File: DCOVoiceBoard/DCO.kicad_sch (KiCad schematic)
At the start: 72 parts, among them Q201 BC857, Q202 BC857, U201 TL074, U202 TL074, U203 MCP4451-104E-ST, U204 TL074, U205 MCP4451-104E-ST, U206 TL072

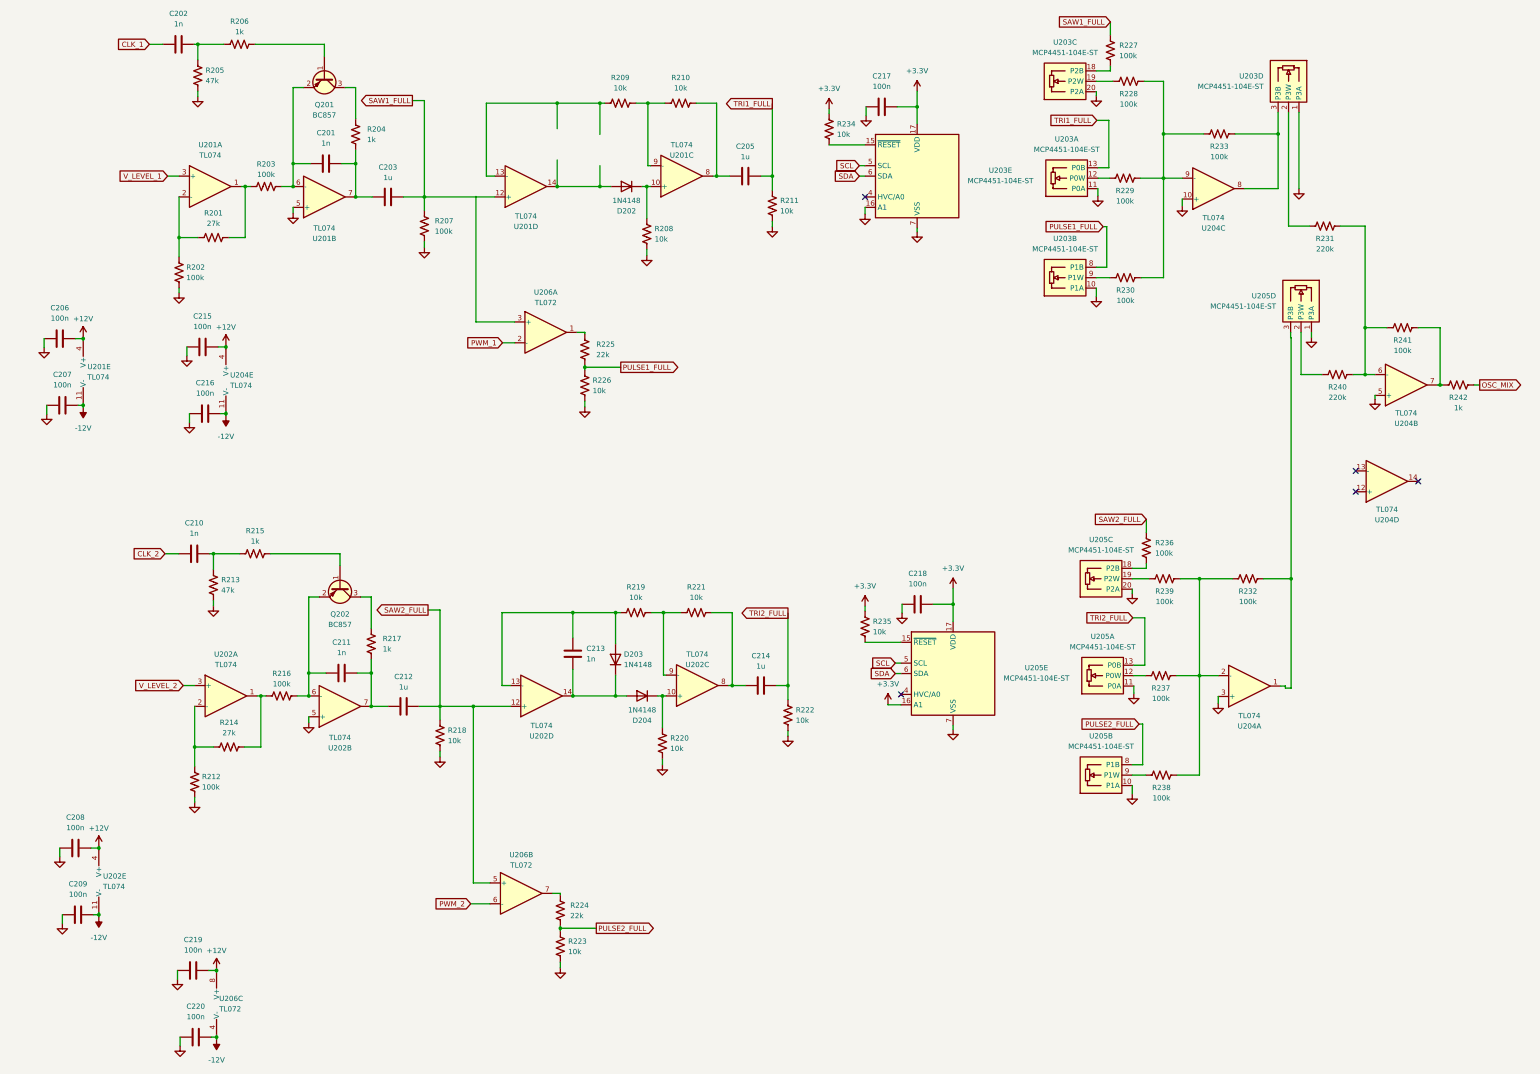
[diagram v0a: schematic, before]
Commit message: voice board rough schematic
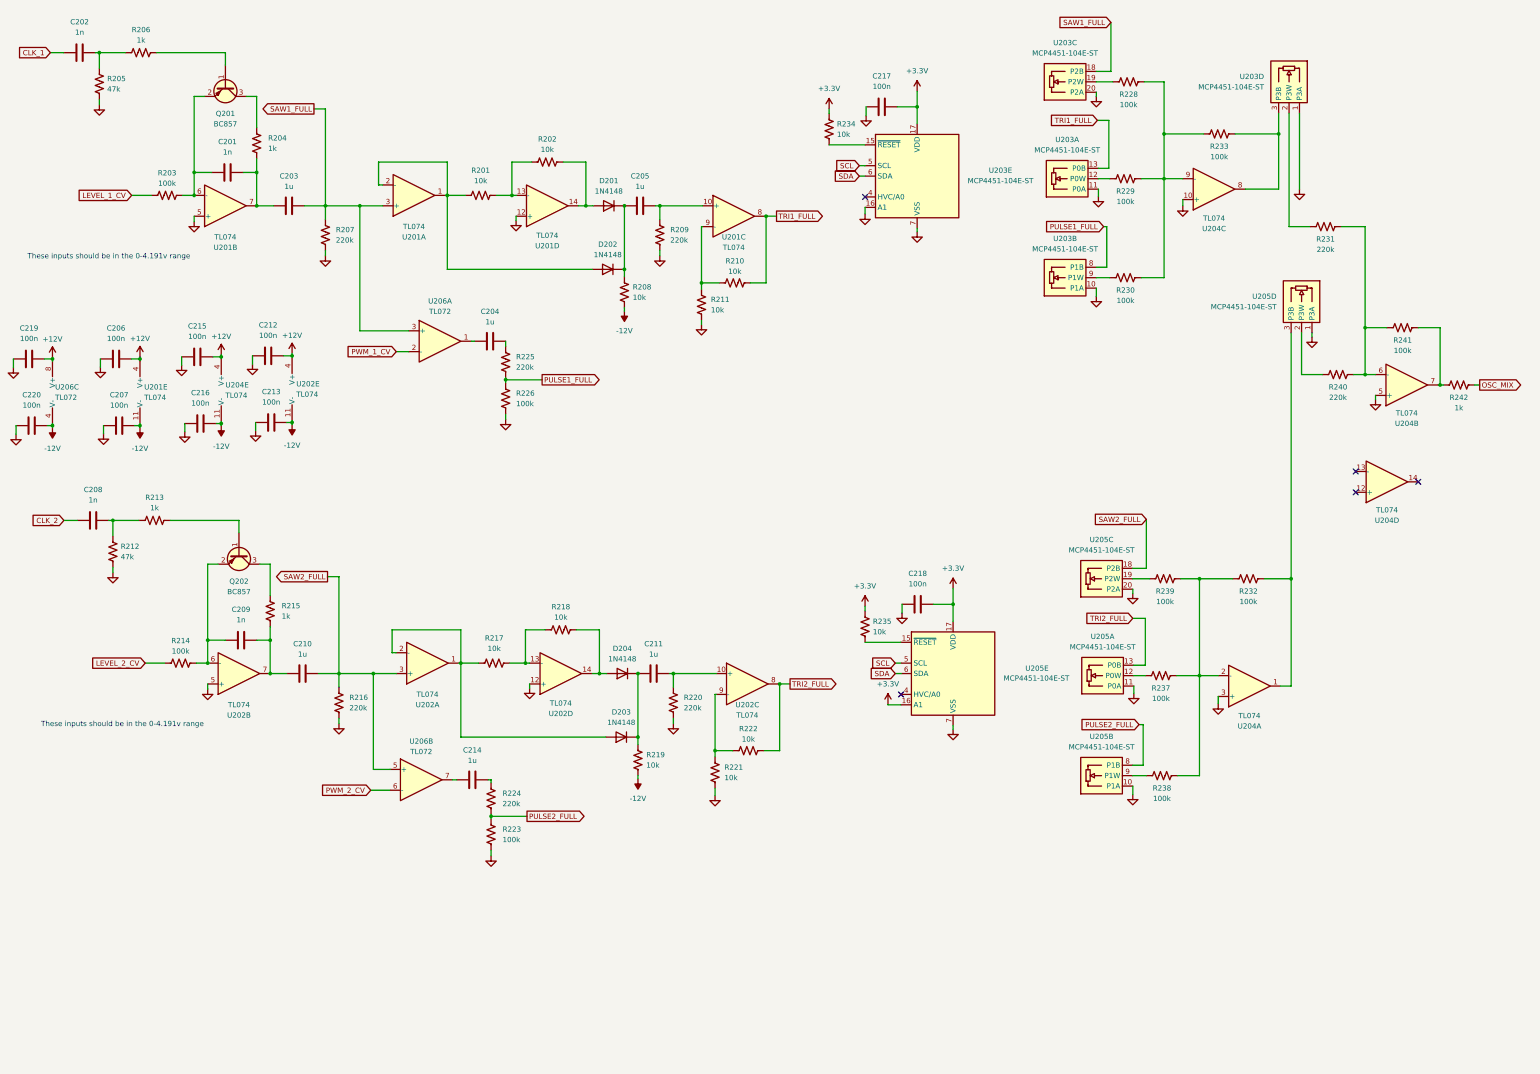
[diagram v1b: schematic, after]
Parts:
- removed R227, R236: 100k, PCM_Resistor_SMD_AKL:R_0805_2012Metric, symbol Device:R_US
- added C204: 1u, Capacitor_SMD:C_0805_2012Metric, symbol Device:C
- added D201: 1N4148, Diode_THT:D_DO-35_SOD27_P7.62mm_Horizontal, symbol Diode:1N4148
- C208, C209: value 100n -> 1n
- C210, C211: value 1n -> 1u
- C212: value 1u -> 100n
- C213: value 1n -> 100n
- D202, D203, D204: footprint Diode_SMD:D_0805_2012Metric -> Diode_THT:D_DO-35_SOD27_P7.62mm_Horizontal
- R201: value 27k -> 10k
- R202: value 100k -> 10k
- R207, R216: value 100k -> 220k
- R209, R220: value 10k -> 220k
- R212: value 100k -> 47k
- R213: value 47k -> 1k
- R214: value 27k -> 100k
- R217: value 1k -> 10k
- R223, R226: value 10k -> 100k
- R224, R225: value 22k -> 220k
- U206: footprint (none) -> Package_SO:SOIC-8_3.9x4.9mm_P1.27mm
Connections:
- net V_LEVEL_1 is gone; now on net SAW1_FULL: U201.3 (+)
- net V_LEVEL_2 is gone; now on net SAW2_FULL: U202.3 (+)
- net +12V: now also C212.2; no longer C208.2
- net -12V: now also C213.2, R208.1, R219.1; no longer C209.2
- net CLK_2: now also C208.1; no longer C210.1
- net GND: now also C212.1, C213.1, R209.2, R211.1, R216.2, R221.1, U201.12 (+), U202.12 (+); no longer C208.1, C209.1, R202.1, R208.2, R211.2, R213.1, R218.2, R222.2
- net SAW1_FULL: now also U203.18 (P2B), U206.3 (+); no longer U201.12 (+)
- net SAW2_FULL: now also C210.2, R216.1, U205.18 (P2B); no longer C212.2, R218.1, U202.12 (+)
- net TRI1_FULL: now also R210.2, U201.8; no longer C205.2, R211.1
- net TRI2_FULL: now also R222.2, U202.8; no longer C214.2, R222.1
- net at R201.1, U201.2 (-): now also D202.2 (A), U201.1; no longer R202.2
- net at R215.1: now also C209.2, C210.1, U202.7; no longer Q202.1 (B)
- net at R210.1, U201.9 (-): now also R211.2; no longer R209.2
- net at Q202.2 (E), U202.6 (-): now also C209.1, R214.2; no longer C211.1, R216.2
- net at R217.2: now also R218.1, U202.13 (-); no longer Q202.3 (C)
- net at U206.7: now also C214.1; no longer R224.1
- net at U206.1: now also C204.1; no longer R225.1
- net at D204.2 (A), U202.14: now also R218.2; no longer C213.1, D203.1 (K)
- net at U201.14: now also R202.2, D201.2 (A); no longer D202.2 (A)
- net at R220.1, U202.10 (+): now also C211.2; no longer D204.1 (K)
- net at R209.1: now also C205.2, U201.10 (+); no longer U201.13 (-)
- net PWM_1 renamed PWM_1_CV
- net PWM_2 renamed PWM_2_CV
- new net: C205.1, D201.1 (K), D202.1 (K), R208.2
- new net: R221.2, R222.1, U202.9 (-)
- new net: C204.2, R225.1
- new net: C211.1, D203.1 (K), D204.1 (K), R219.2
- new net: C208.2, R212.2, R213.2
- new net: Q202.1 (B), R213.1
- new net: Q202.3 (C), R215.2
- new net: C214.2, R224.1
- new net: D203.2 (A), R217.1, U202.1, U202.2 (-)
- new net: R201.2, R202.1, U201.13 (-)
- new net LEVEL_1_CV: R203.1
- new net LEVEL_2_CV: R214.1
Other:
- note added: "These inputs should be in the 0-4.191v range"
- moved on the sheet: C201, C202, C203, C206, C207, C215, C216, C219, C220, Q201, R203, R204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

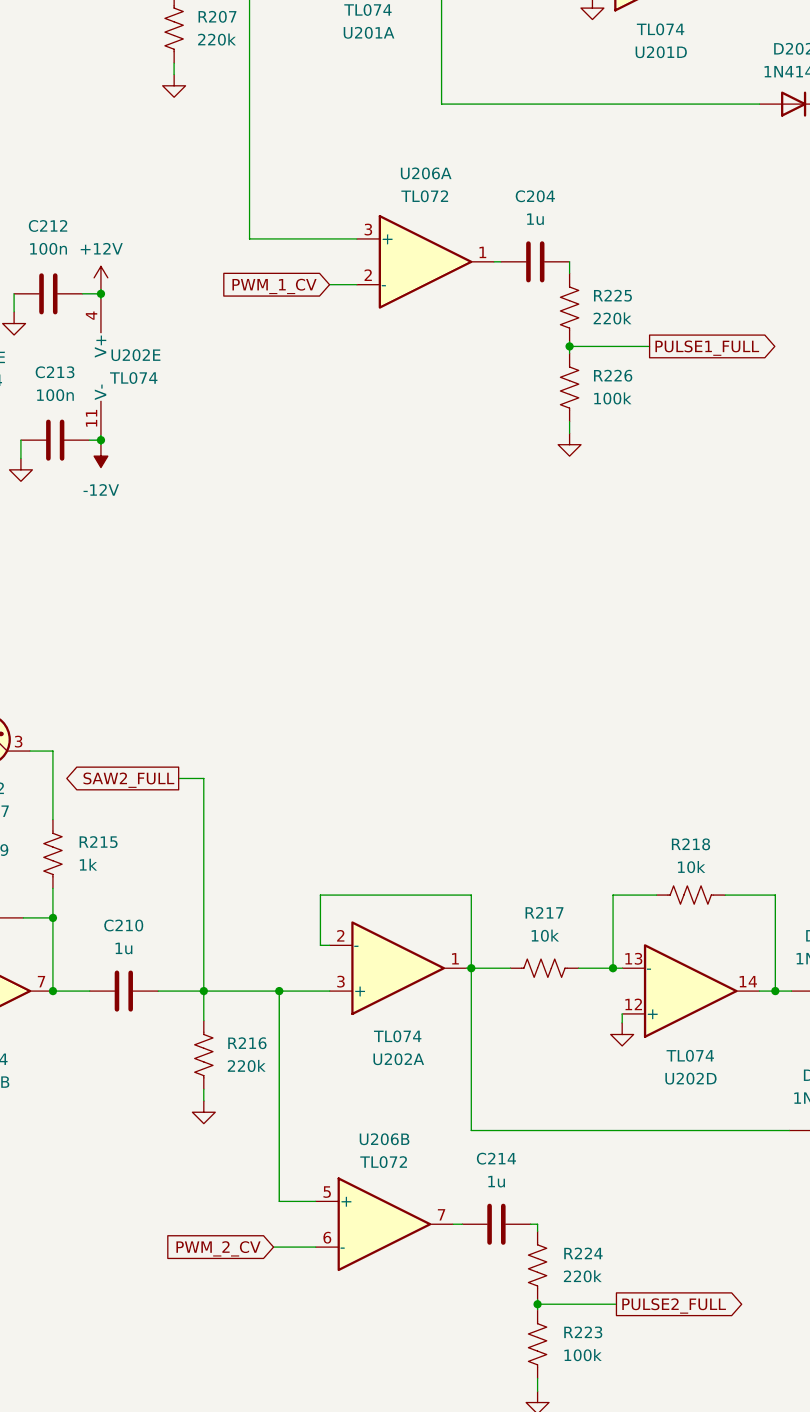
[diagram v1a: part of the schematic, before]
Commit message: net classes, osc layout
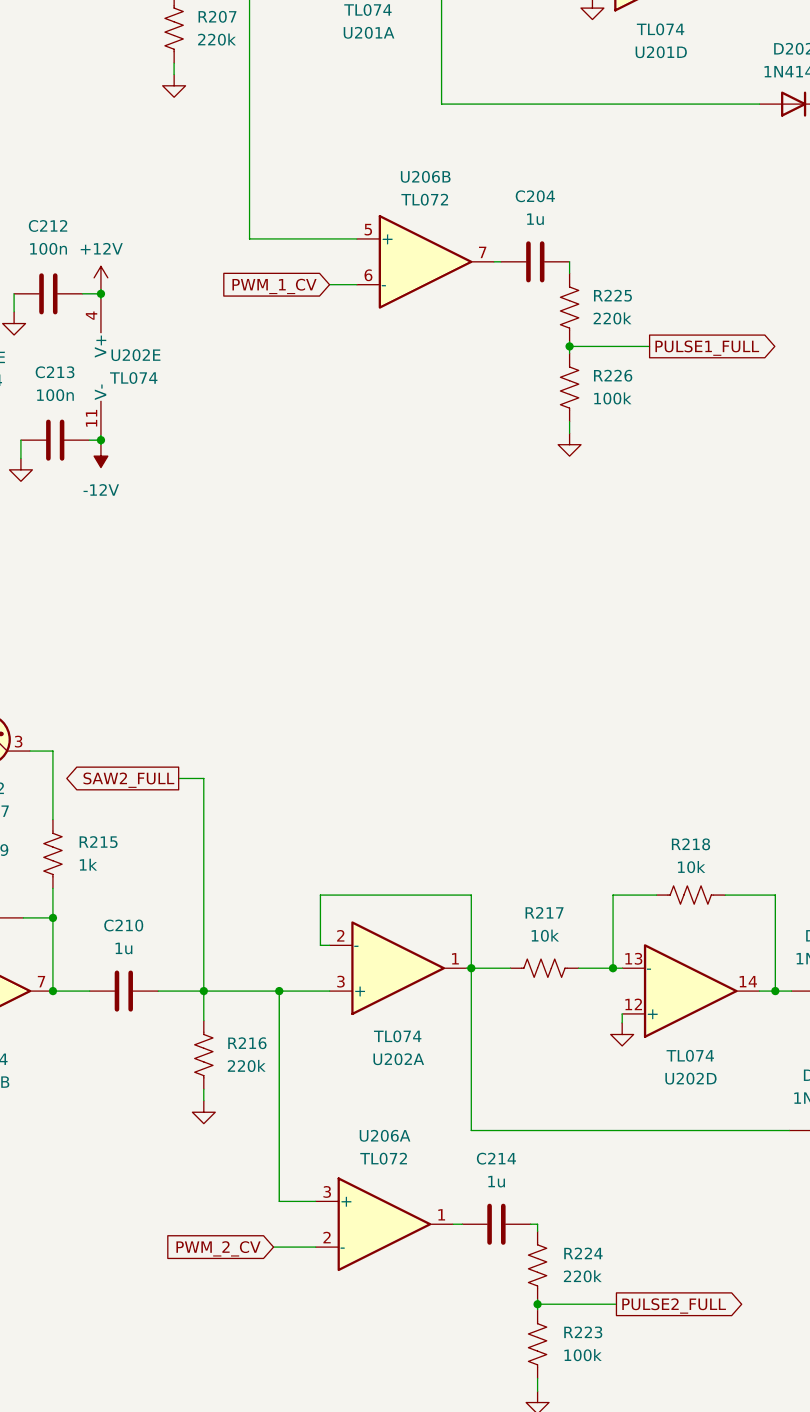
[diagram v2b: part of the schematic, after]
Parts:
- D201, D202, D203, D204: footprint Diode_THT:D_DO-35_SOD27_P7.62mm_Horizontal -> Diode_SMD:D_0805_2012Metric
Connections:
- net PWM_1_CV: now also U206.6 (-); no longer U206.2 (-)
- net PWM_2_CV: now also U206.2 (-); no longer U206.6 (-)
- net SAW1_FULL: now also U206.5 (+); no longer U206.3 (+)
- net SAW2_FULL: now also U206.3 (+); no longer U206.5 (+)
- net at C204.1: now also U206.7; no longer U206.1
- net at C214.1: now also U206.1; no longer U206.7
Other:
- moved on the sheet: U206A, U206B
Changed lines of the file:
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@@
       (effects (font (size 1.27 1.27)))
     )
-    (property "Footprint" "Diode_THT:D_DO-35_SOD27_P7.62mm_Horizontal" (at 160.274 80.772 0)
+    (property "Footprint" "Diode_SMD:D_0805_2012Metric" (at 160.274 80.772 0)
       (effects (font (size 1.27 1.27)) hide)
     )
@@
     )
   )
-  (symbol (lib_id "Amplifier_Operational:TL072") (at 114.808 205.232 0) (unit 2)
-    (in_bom yes) (on_board yes) (dnp no) (fields_autoplaced)
-    (property "Reference" "U206" (at 114.808 195.834 0)
-      (effects (font (size 1.27 1.27)))
-    )
-    (property "Value" "TL072" (at 114.808 198.374 0)
-      (effects (font (size 1.27 1.27)))
-    )
-    (property "Footprint" "Package_SO:SOIC-8_3.9x4.9mm_P1.27mm" (at 114.808 205.232 0)
-      (effects (font (size 1.27 1.27)) hide)
-    )
-    (property "Datasheet" "http://www.ti.com/lit/ds/symlink/tl071.pdf" (at 114.808 205.232 0)
+  (symbol (lib_id "Amplifier_Operational:TL072") (at 119.38 98.298 0) (unit 2)
+    (in_bom yes) (on_board yes) (dnp no) (fields_autoplaced)
+    (property "Reference" "U206" (at 119.38 88.9 0)
+      (effects (font (size 1.27 1.27)))
+    )
+    (property "Value" "TL072" (at 119.38 91.44 0)
+      (effects (font (size 1.27 1.27)))
+    )
+    (property "Footprint" "Package_SO:SOIC-8_3.9x4.9mm_P1.27mm" (at 119.38 98.298 0)
+      (effects (font (size 1.27 1.27)) hide)
+    )
+    (property "Datasheet" "http://www.ti.com/lit/ds/symlink/tl071.pdf" (at 119.38 98.298 0)
       (effects (font (size 1.27 1.27)) hide)
     )
@@
       (effects (font (size 1.27 1.27)))
     )
-    (property "Footprint" "Diode_THT:D_DO-35_SOD27_P7.62mm_Horizontal" (at 160.528 65.278 0)
+    (property "Footprint" "Diode_SMD:D_0805_2012Metric" (at 160.528 65.278 0)
       (effects (font (size 1.27 1.27)) hide)
     )
@@
       (effects (font (size 1.27 1.27)))
     )
-    (property "Footprint" "Diode_THT:D_DO-35_SOD27_P7.62mm_Horizontal" (at 163.576 194.818 0)
+    (property "Footprint" "Diode_SMD:D_0805_2012Metric" (at 163.576 194.818 0)
       (effects (font (size 1.27 1.27)) hide)
     )
@@
     )
   )
-  (symbol (lib_id "Amplifier_Operational:TL072") (at 119.38 98.298 0) (unit 1)
-    (in_bom yes) (on_board yes) (dnp no) (fields_autoplaced)
-    (property "Reference" "U206" (at 119.38 88.519 0)
-      (effects (font (size 1.27 1.27)))
-    )
-    (property "Value" "TL072" (at 119.38 91.059 0)
-      (effects (font (size 1.27 1.27)))
-    )
-    (property "Footprint" "Package_SO:SOIC-8_3.9x4.9mm_P1.27mm" (at 119.38 98.298 0)
-      (effects (font (size 1.27 1.27)) hide)
-    )
-    (property "Datasheet" "http://www.ti.com/lit/ds/symlink/tl071.pdf" (at 119.38 98.298 0)
+  (symbol (lib_id "Amplifier_Operational:TL072") (at 114.808 205.232 0) (unit 1)
+    (in_bom yes) (on_board yes) (dnp no) (fields_autoplaced)
+    (property "Reference" "U206" (at 114.808 195.453 0)
+      (effects (font (size 1.27 1.27)))
+    )
+    (property "Value" "TL072" (at 114.808 197.993 0)
+      (effects (font (size 1.27 1.27)))
+    )
+    (property "Footprint" "Package_SO:SOIC-8_3.9x4.9mm_P1.27mm" (at 114.808 205.232 0)
+      (effects (font (size 1.27 1.27)) hide)
+    )
+    (property "Datasheet" "http://www.ti.com/lit/ds/symlink/tl071.pdf" (at 114.808 205.232 0)
       (effects (font (size 1.27 1.27)) hide)
     )
@@
       (effects (font (size 1.27 1.27)))
     )
-    (property "Footprint" "Diode_THT:D_DO-35_SOD27_P7.62mm_Horizontal" (at 163.83 179.324 0)
-      (effects (font (size 1.27 1.27)) hide)
-    )
+    (property "Footprint" "Diode_SMD:D_0805_2012Metric" (at 163.83 179.324 0)
+      (effects (font (size 1.27 1.27)) hide)
+    )

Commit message: motherboard hardware
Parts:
- removed R234, R235: 10k, PCM_Resistor_SMD_AKL:R_0805_2012Metric, symbol Device:R_US
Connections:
- net +3.3V: now also U203.15 (~{RESET}), U205.15 (~{RESET})
- net TRI1_FULL: now also U203.3 (P3B); no longer U203.13 (P0B)
- net TRI2_FULL: now also U205.3 (P3B); no longer U205.13 (P0B)
- net at R229.1: now also U203.2 (P3W); no longer U203.12 (P0W)
- net at R237.1: now also U205.2 (P3W); no longer U205.12 (P0W)
- net at R233.2, U204.8: now also U203.13 (P0B); no longer U203.3 (P3B)
- net at R240.1: now also U205.12 (P0W); no longer U205.2 (P3W)
- net at R232.2, U204.1: now also U205.13 (P0B); no longer U205.3 (P3B)
- net at R231.1: now also U203.12 (P0W); no longer U203.2 (P3W)
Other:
- moved on the sheet: U203A, U203D, U205A, U205D
